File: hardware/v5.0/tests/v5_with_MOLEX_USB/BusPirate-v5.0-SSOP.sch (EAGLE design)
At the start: 46 parts, among them CON1 CON_HEADER_1X10-RIGHT_ANGLED_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, CON2 CON_HEADER_1X05-PTH, CON3 CON-USB-F-MICRO-B, IC1 PIC24FJ64GA002, IC2 4066, IC4 IC_FT230X-SSOP-16, IC5 IC_BL1551, IC6 IC_BL1551

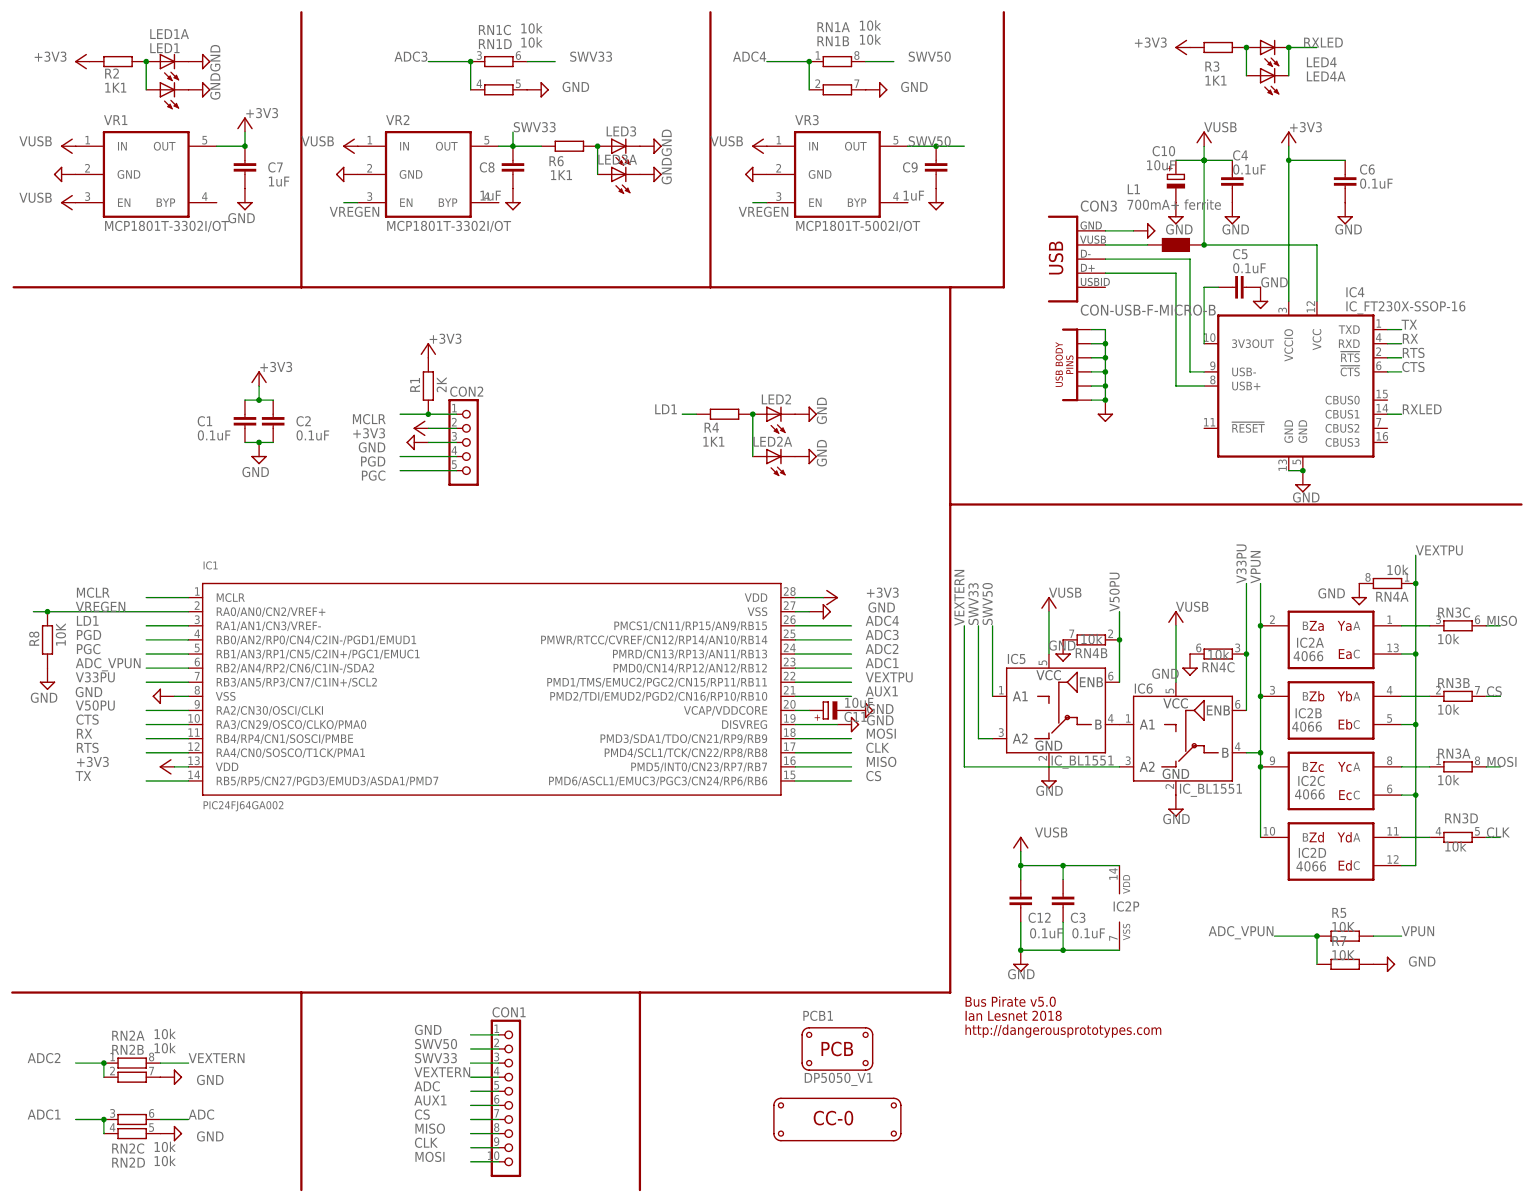
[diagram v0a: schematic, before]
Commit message: Added v5 hardware with different USB Micro B style connectors
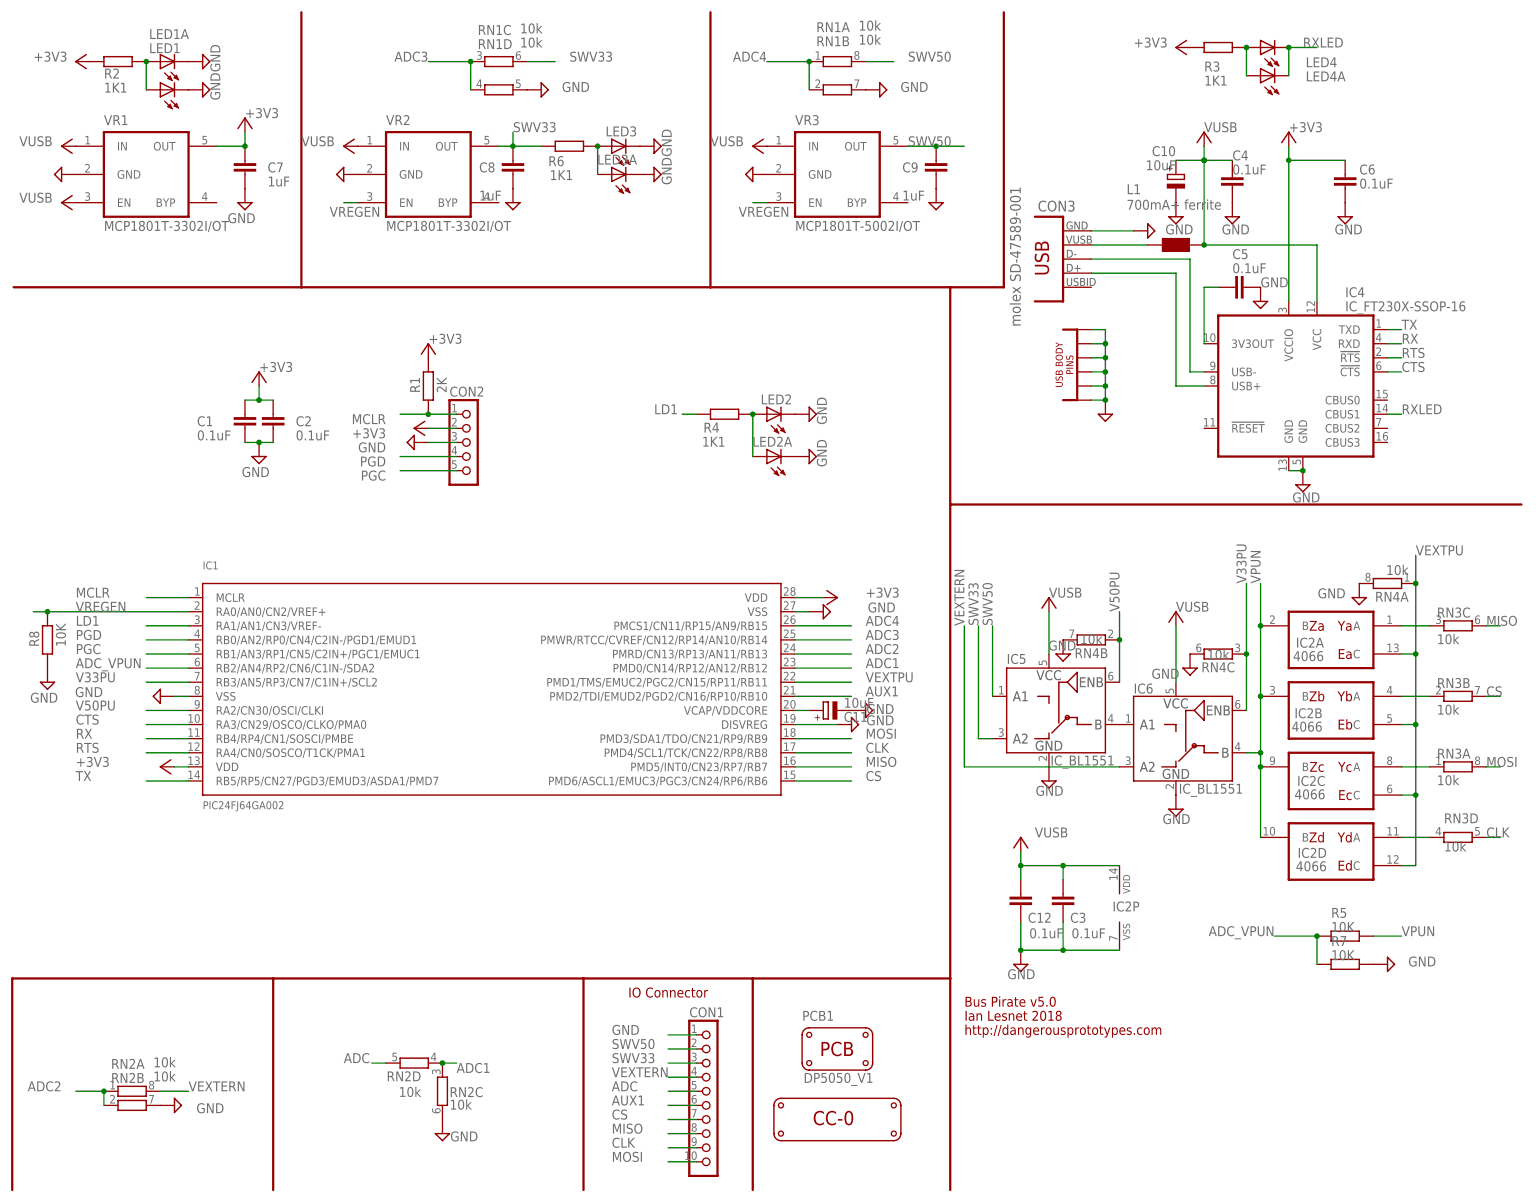
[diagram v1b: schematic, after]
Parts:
- CON3: value CON-USB-F-MICRO-B -> molex SD-47589-001; device dp_devices.v6:CON-USB-F-MICRO-B -> dp_devices.v6:CON-USB-F-MICRO-B-2
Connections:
- net $N26: now also CON3CON.VUSB; no longer CON3CON1.VUSB
- net ADC: now also RN2D.2; no longer RN2C.2
- net GND: now also CON3BGND.P$1, CON3BGND.P$2, CON3BGND.P$3, CON3BGND.P$4, CON3BGND.P$5, CON3BGND.P$6, CON3CON.GND, RN2C.2; no longer CON3CON1.GND, CON3GPINS.P$1, CON3GPINS.P$2, CON3GPINS.P$3, CON3GPINS.P$4, CON3GPINS.P$5, CON3GPINS.P$6, RN2D.2
- net N$15: now also CON3CON.D+; no longer CON3CON1.D+
- net N$16: now also CON3CON.D-; no longer CON3CON1.D-
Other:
- note added: "IO Connector"
- moved on the sheet: CON1, RN2A, RN2B, RN2C, RN2D
